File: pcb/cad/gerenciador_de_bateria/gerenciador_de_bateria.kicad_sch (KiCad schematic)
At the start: 31 parts, among them J1 Conn_01x02_Male, J14 Conn_01x03_Male, J2 Conn_01x03_Male, J3 Conn_01x02_Male, SW1 SW_Push, U1 USB_BQ25629, U2 BQ25629

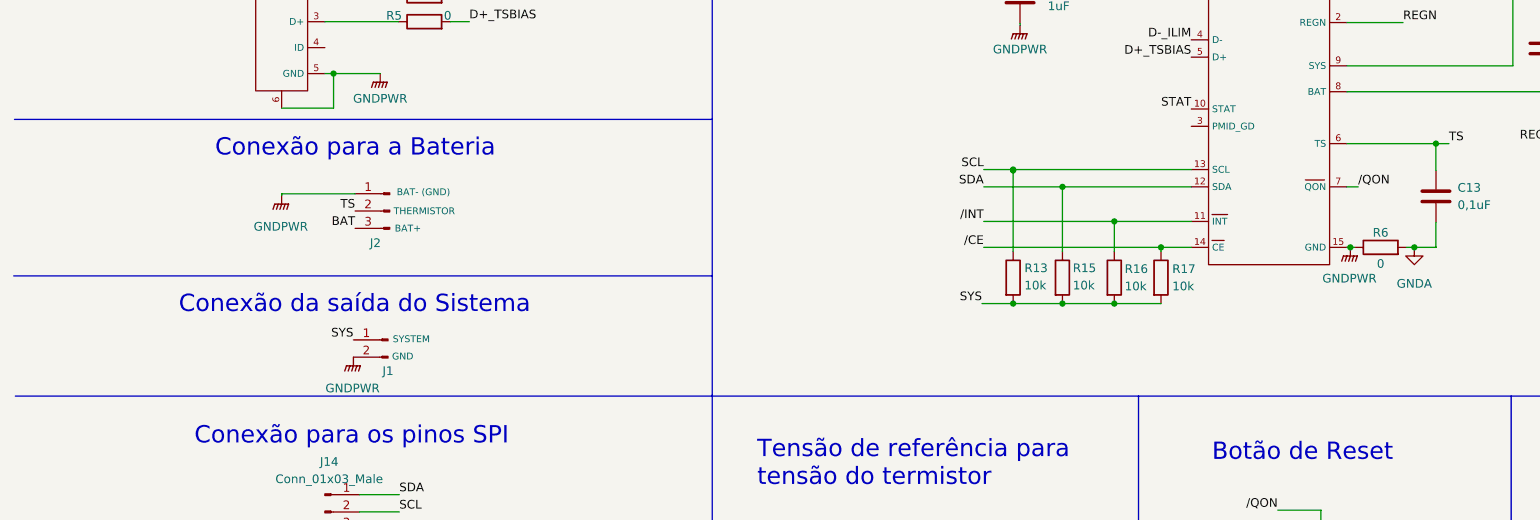
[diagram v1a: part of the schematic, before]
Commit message: Alteração dos conectores no esquemático para o rearranjo e a diminuição da PCB que foi feita no gerenciador_de_bateria
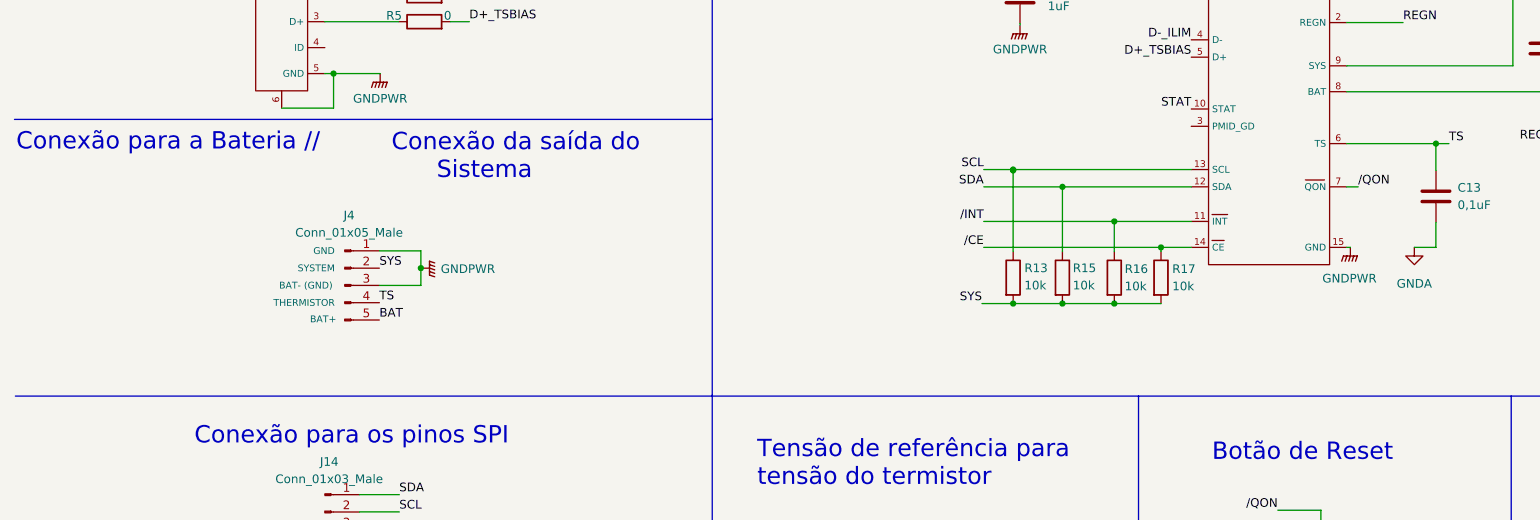
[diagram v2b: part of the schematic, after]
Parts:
- removed J1: Conn_01x02_Male, Connector_PinHeader_2.54mm:PinHeader_1x02_P2.54mm_Vertical, symbol Connector:Conn_01x02_Male
- removed J2: Conn_01x03_Male, Connector_PinHeader_2.54mm:PinHeader_1x03_P2.54mm_Vertical, symbol Connector:Conn_01x03_Male
- removed R6: 0, Resistor_SMD:R_0805_2012Metric, symbol Device:R
- added J4: Conn_01x05_Male, Connector_PinHeader_2.54mm:PinHeader_1x05_P2.54mm_Vertical, symbol Connector:Conn_01x05_Male
- SW1: footprint Button_Switch_THT:SW_PUSH_6mm -> Button_Switch_SMD:SW_SPST_B3U-1000P
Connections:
- net BAT: now also J4.5 (Pin_5)
- net GNDPWR: now also J4.1 (Pin_1), J4.3 (Pin_3)
- net SYS: now also J4.2 (Pin_2)
- net TS: now also J4.4 (Pin_4)
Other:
- note added: "Conexão para a Bateria //"
- note removed: "Conexão para a Bateria"
